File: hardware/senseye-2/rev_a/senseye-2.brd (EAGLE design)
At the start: 149.8 x 55.3 mm, 17 parts, among them U1 ADC121S101, U2 ADC121S101, U3 ADC121S101

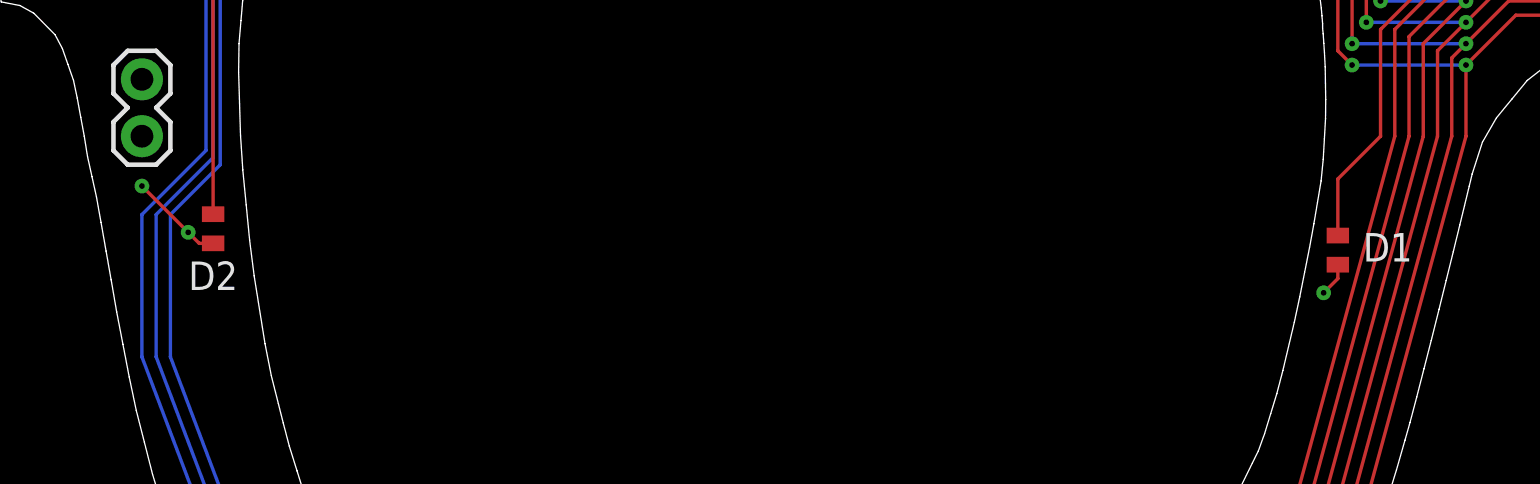
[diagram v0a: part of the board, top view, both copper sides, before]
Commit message: added inline resistors for diodes
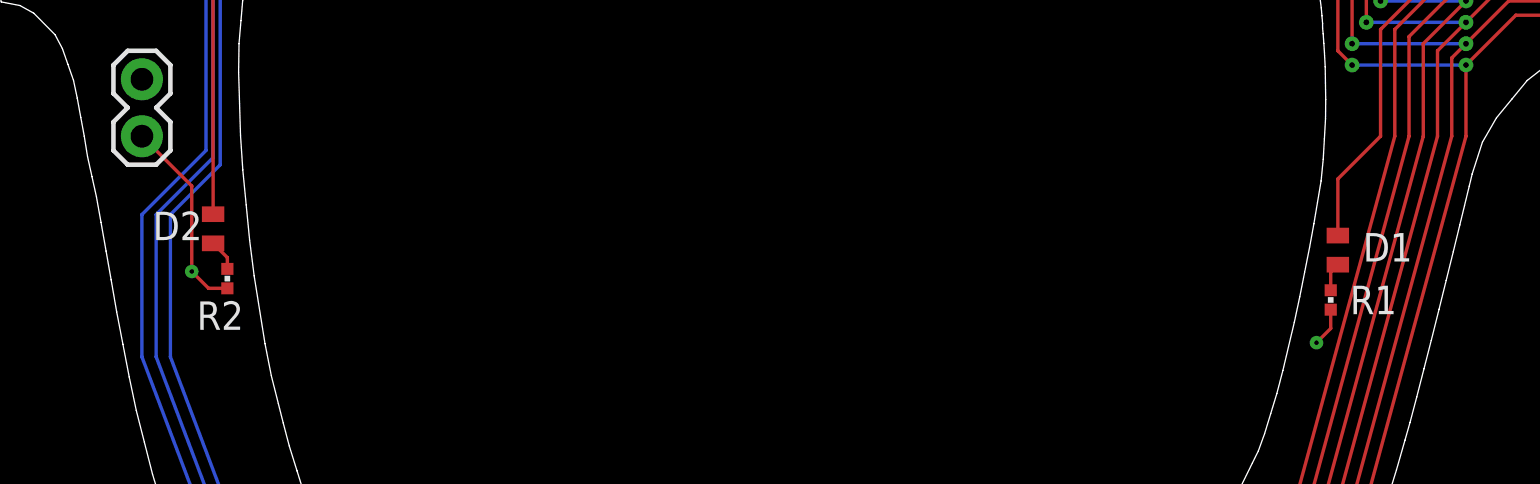
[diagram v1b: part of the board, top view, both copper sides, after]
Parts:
- removed C5: 1u, passives:0402_CAP
- added C2: 1u, passives:0402_CAP
- added R4, R5: 10k, passives:0402_RES
- R1, R2: value 10k -> 470
- moved C3 51.1 mm to (46.7, -6.75)
- moved R3 42.6 mm to (62.2, -8.89)
- moved R2 25.1 mm to (11.7, -28.6), flipped to the top
- moved R1 20.7 mm to (61.0, -29.5), flipped to the top
- renumbered JP6 to JP5
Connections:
- new net N$2: D1.1, R1.2
- new net N$5: D2.1, R2.2
- net ANALOG0: now also R3.1; no longer R1.1
- net GND: now also C2.1, R4.2, R5.2; no longer C5.1, R1.2, R2.2
- net N$1: now also R4.1; no longer R2.1
- net N$3: now also R5.1; no longer R3.1
- net VCC: now also C2.2, R1.1, R2.1; no longer C5.2, D1.1, D2.1
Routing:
- net VCC: track 62.0 -> 66.9 mm, vias 12 -> 11
- net N$5: track 0.00 -> 1.40 mm
- net N$2: track 0.00 -> 1.27 mm
